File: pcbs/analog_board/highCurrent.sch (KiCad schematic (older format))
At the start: 26 parts, among them P2 CONN_01X03, P3 CONN_01X03, P4 CONN_01X03, P5 CONN_01X03, Q1 MMBT3904, U1 AD8616

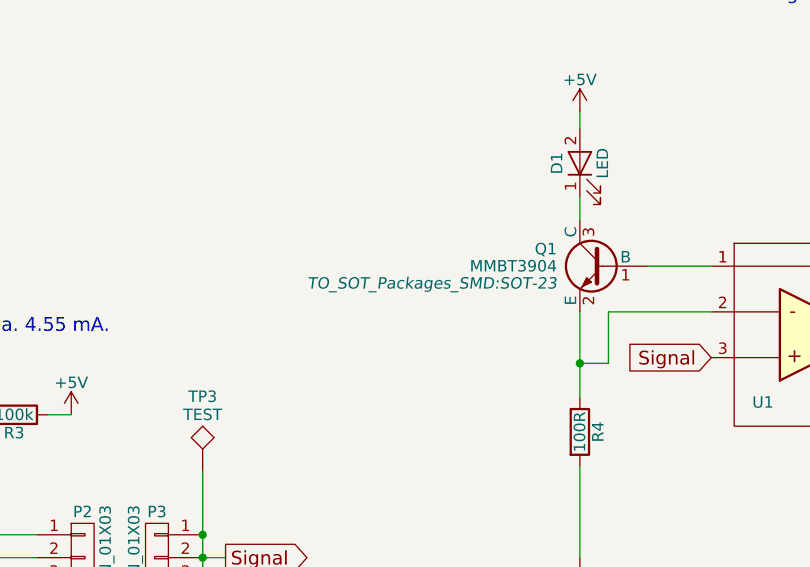
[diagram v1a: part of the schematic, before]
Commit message: Almost done with the etching machine CAD work.
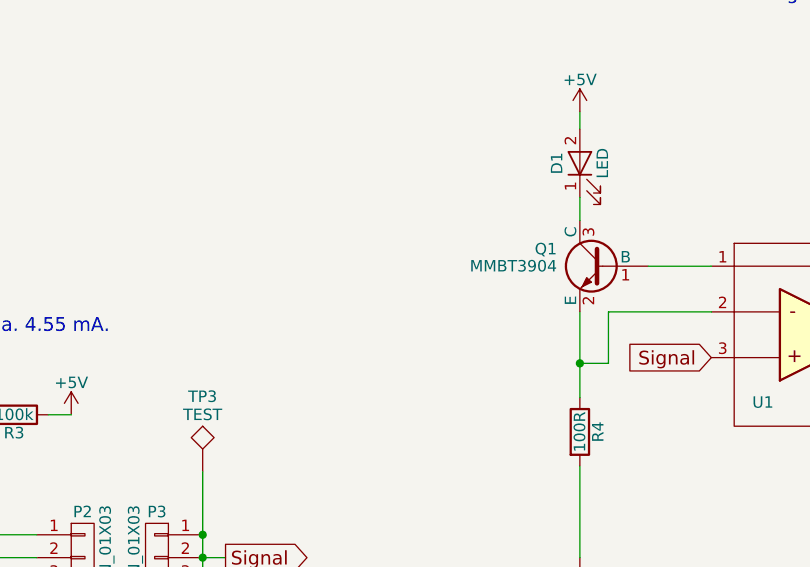
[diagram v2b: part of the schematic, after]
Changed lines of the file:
@@
 F 0 "Q1" H 5600 3950 50  0000 L CNN
 F 1 "MMBT3904" H 5600 3875 50  0000 L CNN
-F 2 "TO_SOT_Packages_SMD:SOT-23" H 5600 3800 50  0000 L CIN
-F 3 "http://www.nxp.com/packings/SOT23_215.html" H 5400 3875 50  0001 L CNN
+F 2 "TO_SOT_Packages_SMD:SOT-23" H 5600 3800 50  0001 L CIN
+F 3 "https://www.fairchildsemi.com/datasheets/MM/MMBT3904.pdf" H 5400 3875 50  0001 L CNN
 F 4 "1757936RL" H 5400 3875 60  0001 C CNN "Farnell"
 	1    5400 3875
